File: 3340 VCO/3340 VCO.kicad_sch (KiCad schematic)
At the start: 105 parts

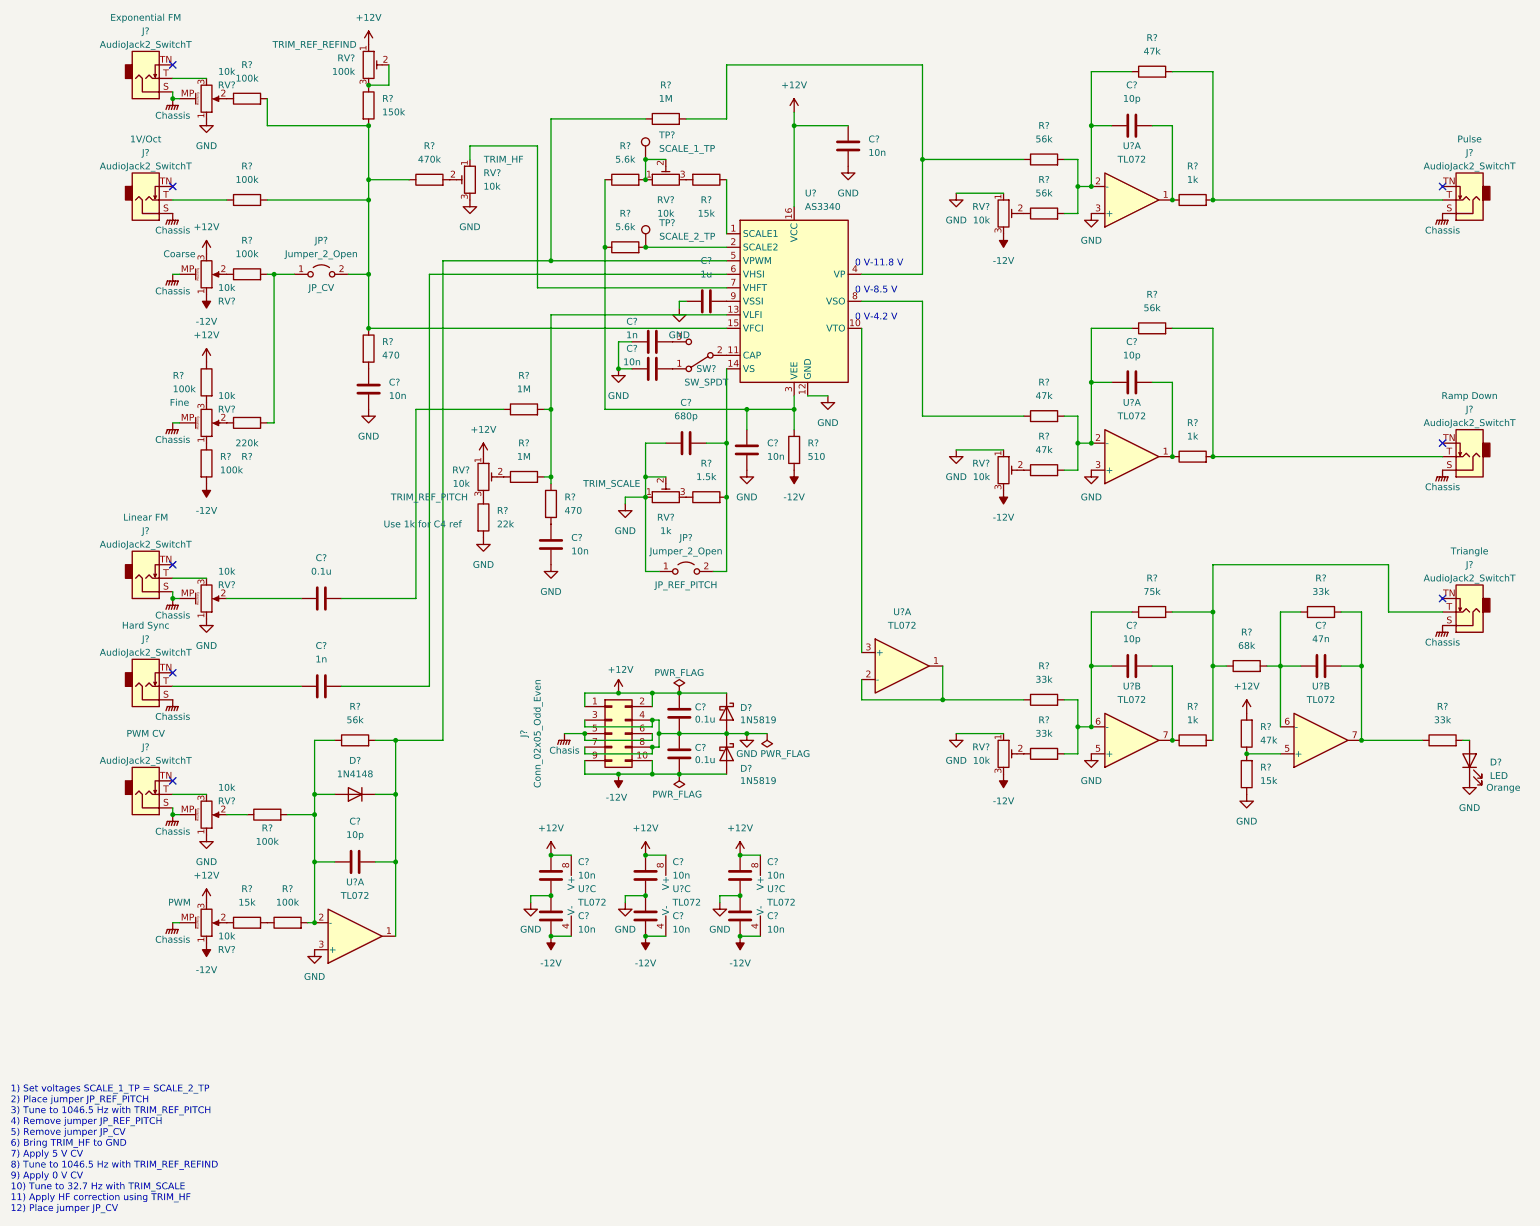
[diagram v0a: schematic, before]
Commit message: Fix VCO ERC issues
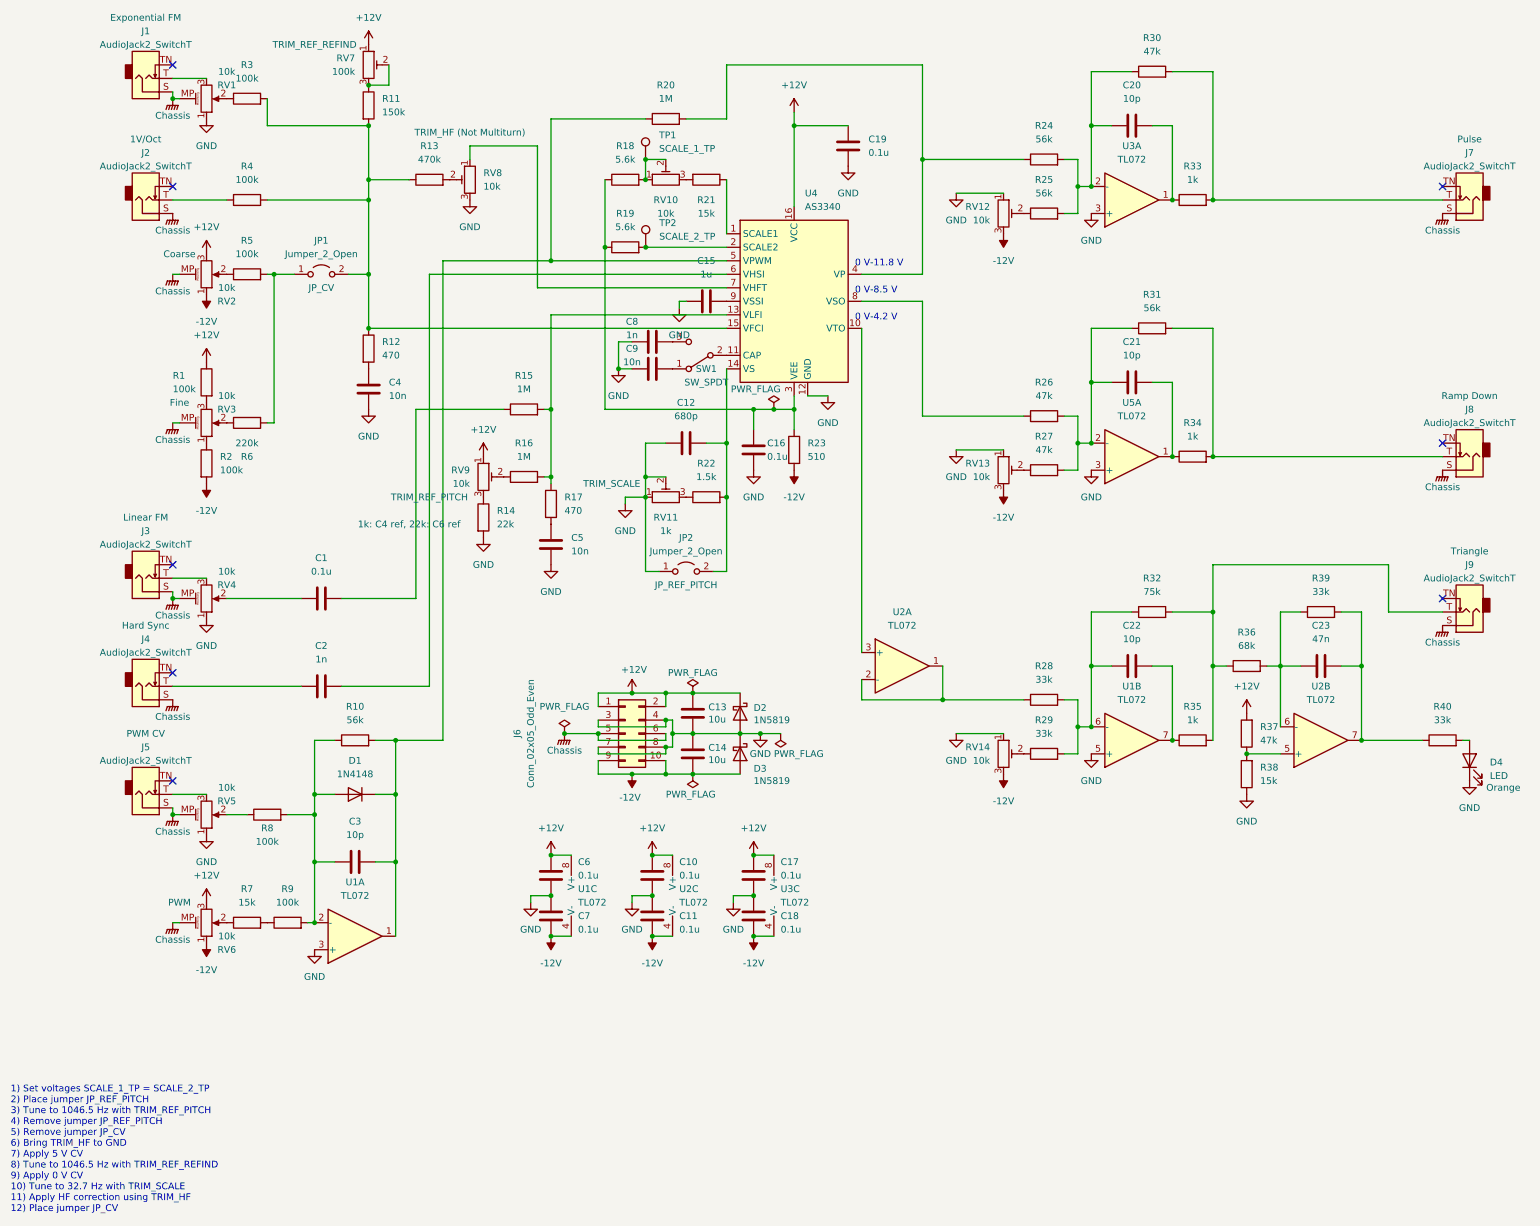
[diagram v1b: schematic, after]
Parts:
- removed C? (x4): 10n, symbol Device:C
- removed U? (x2): TL072, symbol Amplifier_Operational:TL072
- added C10, C11, C17, C18: 0.1u, symbol Device:C
- added unit 3 of U2
- added unit 3 of U3
- C13, C14: renamed from C?; value 0.1u -> 10u
- C16, C19, C6, C7: renamed from C?; value 10n -> 0.1u
- R14: renamed from R?; Notes Use 1k for C4 ref -> 1k: C4 ref, 22k: C6 ref
- RV8: renamed from RV?; Notes TRIM_HF -> TRIM_HF (Not Multiturn)
- gave numbers to parts that had none: 88
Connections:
- net Chasis is gone; now on net Chassis: J6.5 (Pin_5), J6.6 (Pin_6)
- net +12V: now also C10.2, C17.2, U2.8 (V+), U3.8 (V+)
- net -12V: now also C11.1, C18.1, U2.4 (V-), U3.4 (V-)
- net GND: now also C10.1, C11.2, C17.1, C18.2
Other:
- moved on the sheet: C13, C14, C16, D2, D3, J6

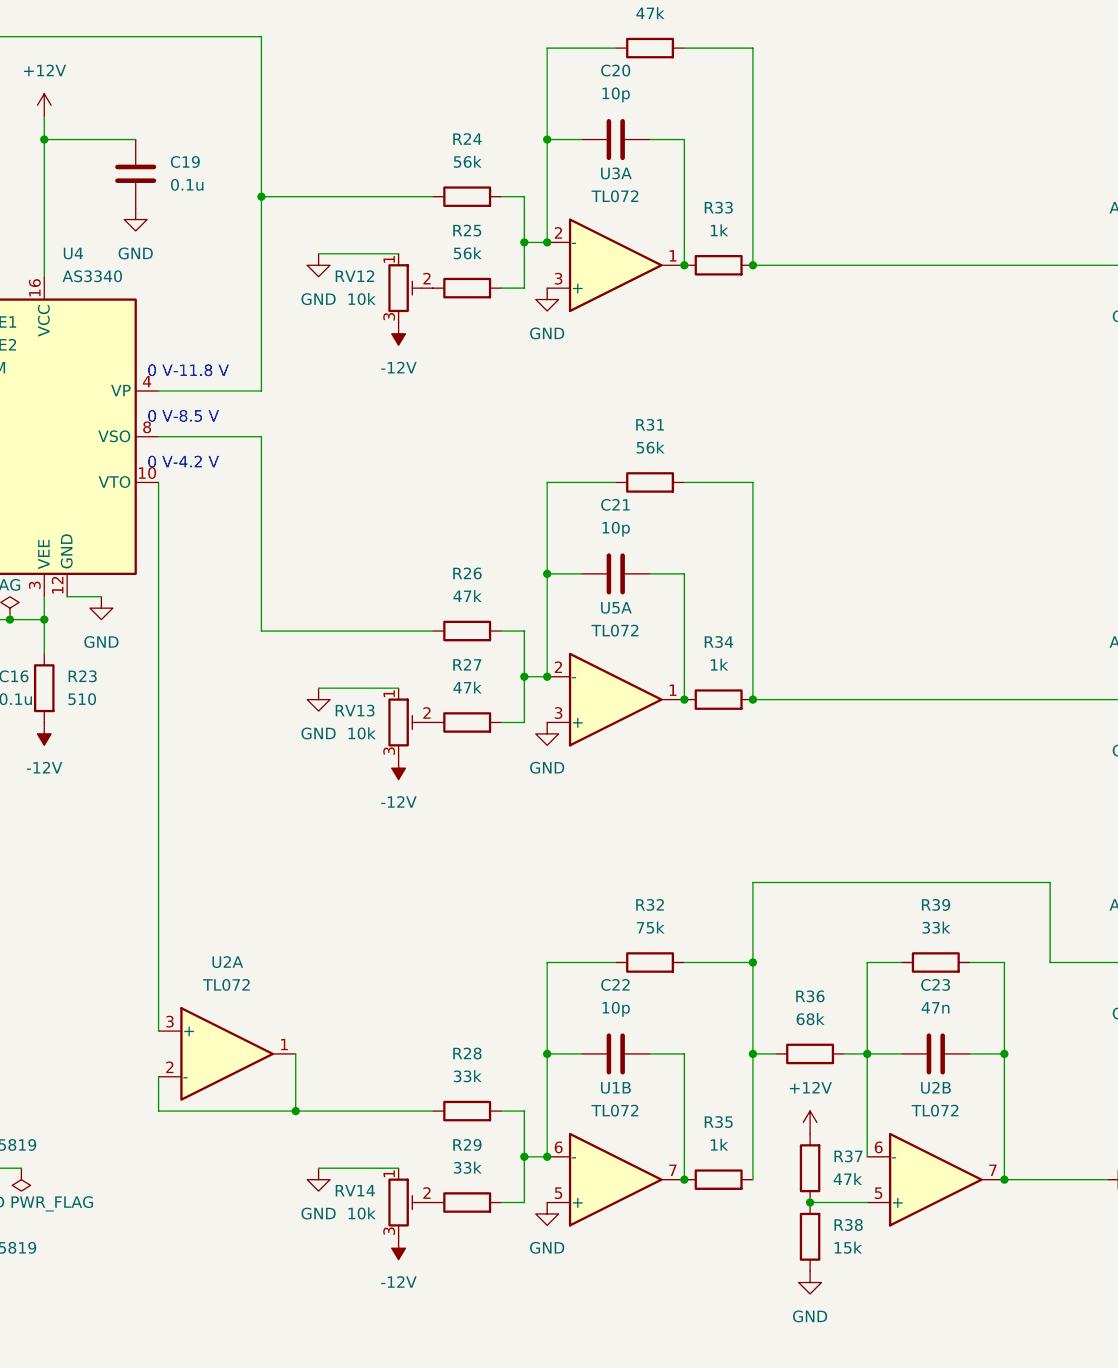
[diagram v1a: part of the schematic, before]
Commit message: Assign footprints
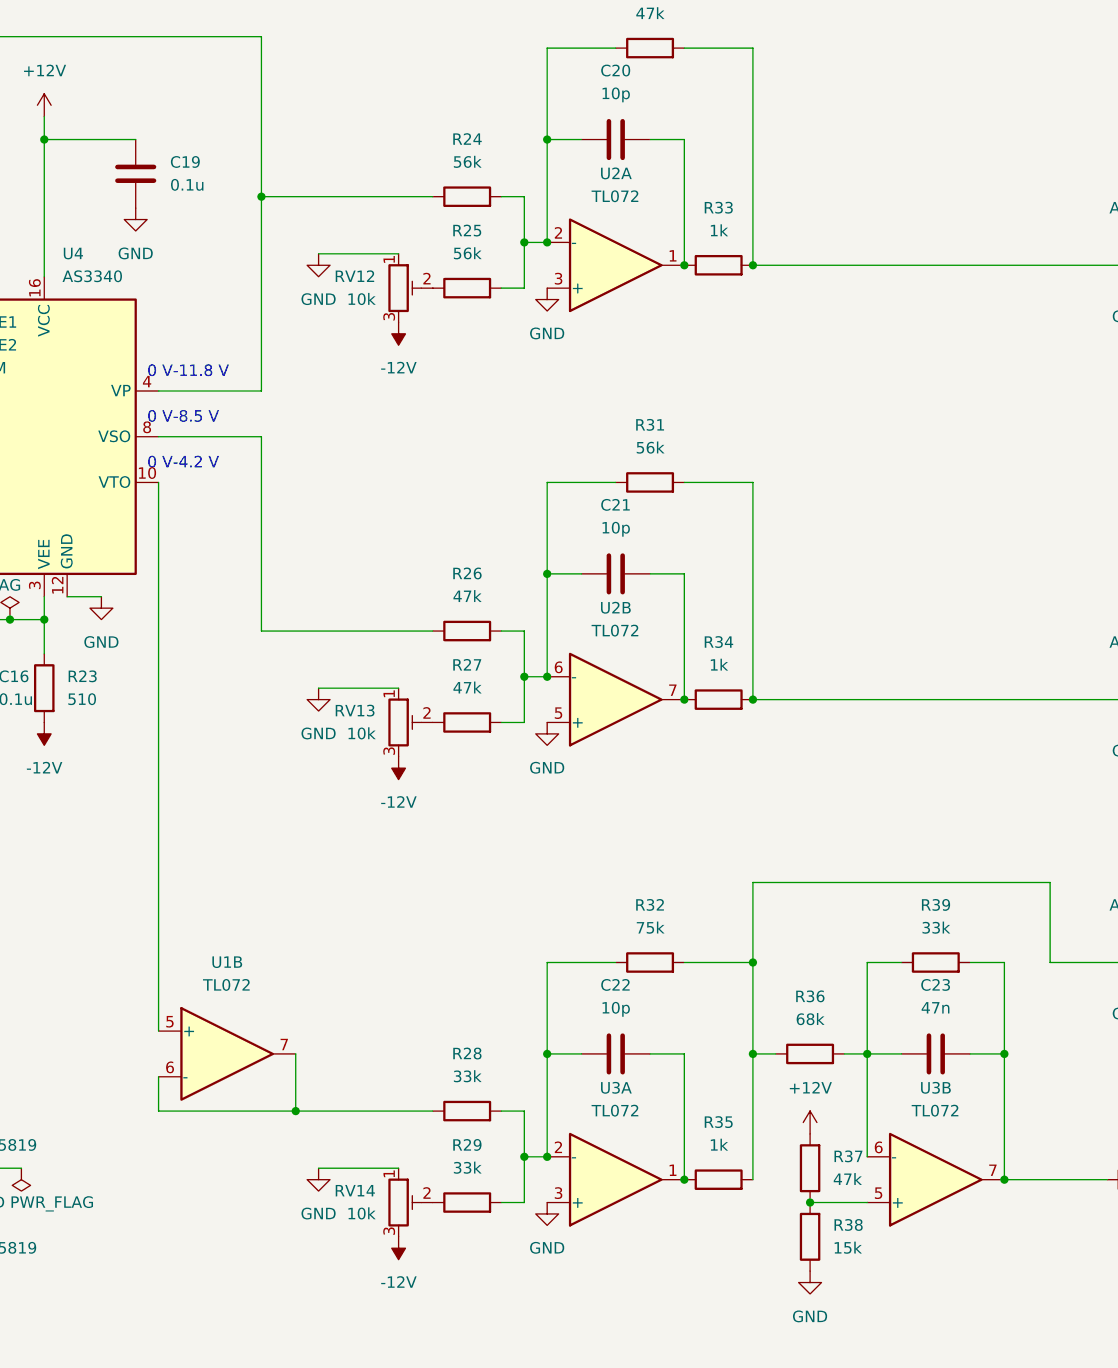
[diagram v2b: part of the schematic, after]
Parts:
- C1, C10, C11, C12, C16, C17, C18, C19, C2, C20, C21, C22, C23, C3, C4, C5, C6, C7, C8, C9: footprint (none) -> 0_Capacitor_THT:C_Disc_D5.5mm_W2.5mm_P2.50mm
- C13, C14: footprint Capacitor_THT:C_Disc_D5.0mm_W2.5mm_P5.00mm -> 0_Capacitor_THT:C_Disc_D5.5mm_W4.0mm_P2.50mm
- C15: footprint (none) -> 0_Capacitor_THT:C_Disc_D5.5mm_W4.0mm_P2.50mm
- D4: footprint (none) -> LED_THT:LED_D5.0mm
- J6: footprint Connector_PinHeader_2.54mm:PinHeader_2x05_P2.54mm_Vertical -> Connector_Molex:Molex_Mini-Fit_Jr_5566-10A_2x05_P4.20mm_Vertical
- JP1, JP2: footprint (none) -> Connector_PinHeader_2.54mm:PinHeader_1x02_P2.54mm_Vertical
- R1, R10, R11, R12, R13, R14, R15, R16, R17, R18, R19, R2, R20, R21, R22, R23, R24, R25, R26, R27, R28, R29, R3, R30, R31, R32, R33, R34, R35, R36, R37, R38, R39, R4, R40, R5, R6, R7, R8, R9: footprint (none) -> Resistor_THT:R_Axial_DIN0207_L6.3mm_D2.5mm_P7.62mm_Horizontal
- RV1, RV2, RV3, RV4, RV5, RV6: footprint (none) -> 0_Potentiometer_THT:Potentiometer_Alpha_RD901F-40-00D_Single_Vertical_MP
- RV10, RV11, RV12, RV13, RV14, RV7, RV9: footprint (none) -> Potentiometer_THT:Potentiometer_Bourns_3296W_Vertical
- RV8: footprint (none) -> Potentiometer_THT:Potentiometer_Runtron_RM-065_Vertical
- SW1: footprint (none) -> 0_Switch_THT:MTS-102_MTS-103_MTS-112_MTS-113_MTS-123
- TP1, TP2: footprint (none) -> Connector_PinHeader_2.54mm:PinHeader_1x01_P2.54mm_Vertical
- U1, U2, U3: footprint (none) -> Package_DIP:DIP-8_W7.62mm_Socket
- U1, U3: renamed from U2; footprint (none) -> Package_DIP:DIP-8_W7.62mm_Socket
- U2: renamed from U3; footprint (none) -> Package_DIP:DIP-8_W7.62mm_Socket
- U2: renamed from U5; footprint (none) -> Package_DIP:DIP-8_W7.62mm_Socket
- U3: renamed from U1; footprint (none) -> Package_DIP:DIP-8_W7.62mm_Socket
- U4: footprint (none) -> Package_DIP:DIP-16_W7.62mm_Socket
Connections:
- net GND: now also U2.5 (+), U3.3 (+); no longer U2.3 (+), U3.5 (+)
- net at C21.1, R26.2, R27.2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: now also U2.6 (-); no longer U2.2 (-)
- net at U4.10 (VTO): now also U1.5 (+); no longer U1.3 (+)
- net at C22.1, R28.2, R29.2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: now also U3.2 (-); no longer U3.6 (-)
- net at C21.2, R34.1: now also U2.7; no longer U2.1
- net at C22.2, R35.1: now also U3.1; no longer U3.7
- new net: R28.1, U1.6 (-), U1.7
